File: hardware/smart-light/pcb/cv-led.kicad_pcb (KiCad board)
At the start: 2 copper layers, 95.7 x 68 mm, 46 parts, among them J1 2P 5.08mm + barrel, J2 5P 5.08mm, J3 2P 5.08mm, K1 SRD-05VDC-SL-C, Q1 AO3400 / IRLZ44N, Q2 AO3400 / IRLZ44N, Q3 AO3400 / IRLZ44N, Q4 AO3400 / IRLZ44N, Q5 S8050, SW1 Tactile 6mm, U1 ESP32-WROOM-32E (4MB), U2 AMS1117-3.3, U3 MP1584 buck

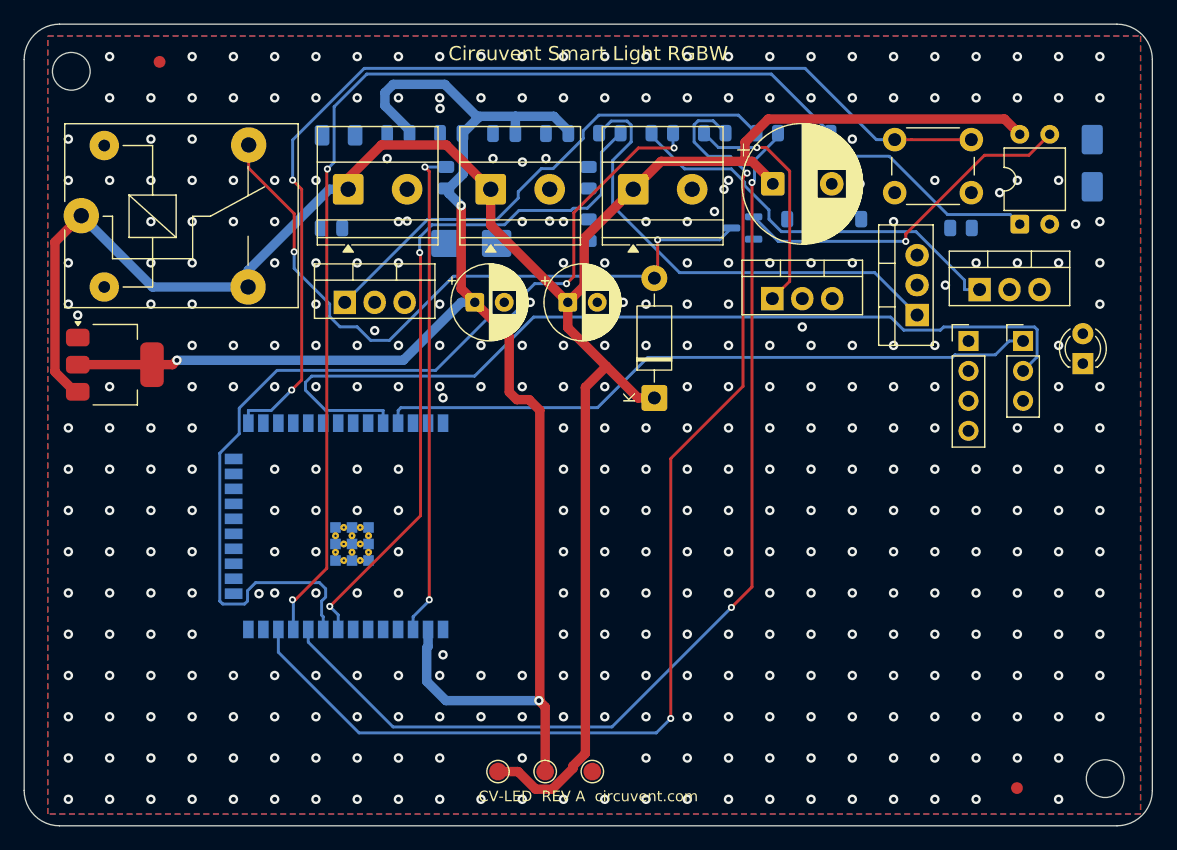
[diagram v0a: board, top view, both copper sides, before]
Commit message: hardware: fix mains isolation barrier gaps, add load-controller PCB
Adds the 13th board (ultra-compact dual-channel load controller: ESP32-C3,
opto+relay channel, MOSFET PWM channel, USB-C, AP2112K LDO, USBLC6 ESD) and
regenerates all 12 existing boards, which were stale with respect to earlier
relay-pinout and LED-polarity fixes.

The substantive change is to the mains isolation barrier. It is a keepout band
the router must not cross, deliberately cut where a component straddles it
because there the isolation is provided by the part's package. Three linked
defects made those cuts unsafe, each only visible once the previous was fixed:

1. The cut removed the barrier across the full band width for the straddling
   part's whole height, while the ISO_BRIDGE area that excuses the gap covered
   only the part itself. The router used the leftover strip beside the part to
   bring +5V within 6.99 mm of AC_N against an 8.0 mm reinforced creepage rule.
2. Straddling parts can overlap in y, so cutting per part put one part's
   keepout on another part's pads. The exempt x-ranges are now unioned per
   strip by a sweep line.
3. The rule only relaxes for items insideArea('ISO_BRIDGE'). With the hole the
   same size as the area, a track could hug the hole's edge without being
   contained in it, so the rule fired anyway and the router had no way to know.
   The hole is now the part's pad bbox + 0.3 mm, strictly inside ISO_BRIDGE at
   the footprint bbox + 0.6 mm.

The tighter hole leaves mains nets less room to reach bridge pads, so some
boards report more unconnected items. That is deliberate: those are documented
hand-routing items, whereas a creepage violation is a safety defect.

Also fixed in the generator:
- _pad_shape() derived a pad's layers from PAD::GetLayer(), which returns F.Cu
  even for pads on B.Cu. Every back-side pad became a phantom obstacle on the
  front, blocking legal paths there while hiding the real one behind. Only
  IsOnLayer() is truthful.
- Castella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
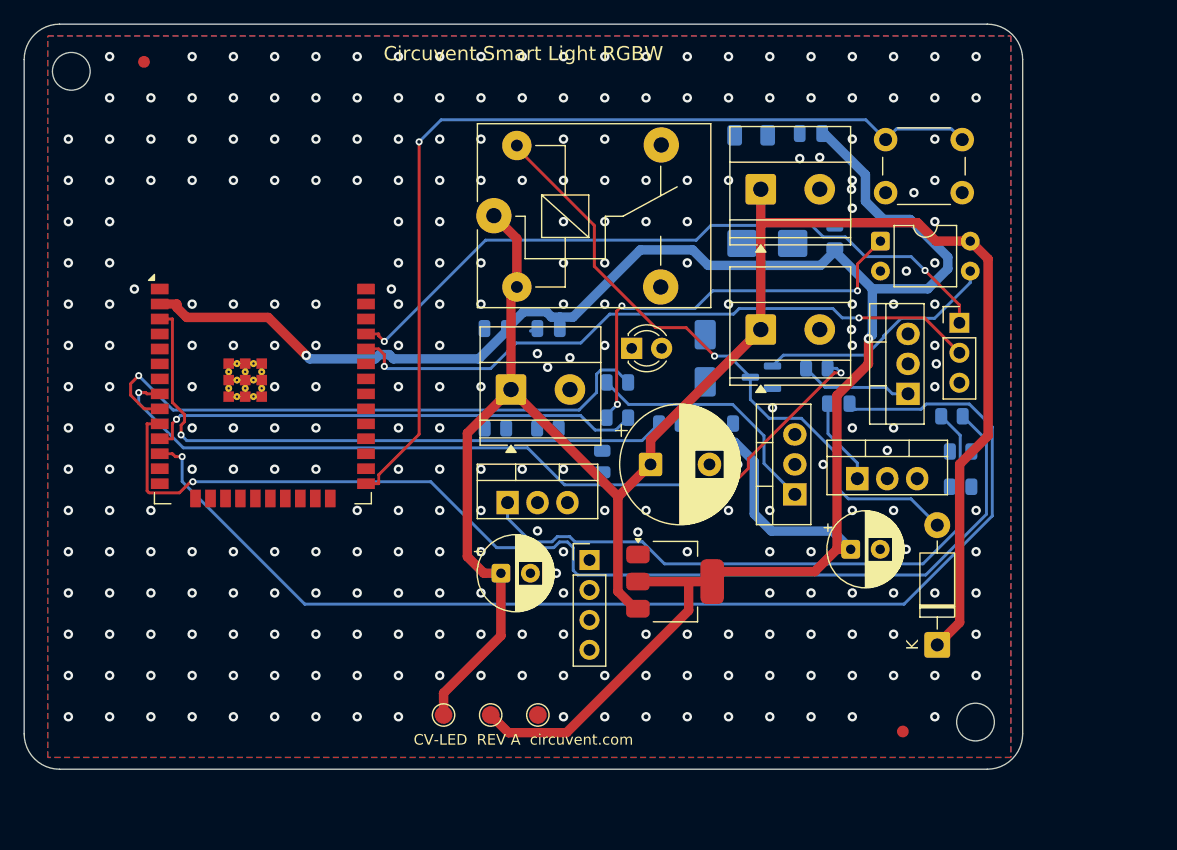
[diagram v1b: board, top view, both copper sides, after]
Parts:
- U1: moved to F.Cu
- moved R12 57.7 mm to (179.4, 119.2)
- moved U2 51.0 mm to (155.2, 127.3)
- moved LED0 38.3 mm to (151.5, 107.5), turned to 0 degrees
- moved C2 38.2 mm to (170.1, 124.5)
- moved U3 37.1 mm to (148.0, 125.5)
- moved D2 36.8 mm to (157.8, 108.3)
- moved R10 36.7 mm to (179.4, 116.2), turned to 180 degrees
- moved R11 36.3 mm to (149.0, 117.1), turned to 90 degrees
- moved J1 35.0 mm to (162.5, 94.0)
- moved C4 35.0 mm to (166.7, 89.3)
- moved K1 35.0 mm to (139.8, 96.2)
- moved F1 35.0 mm to (161.7, 89.4)
- moved C5 33.7 mm to (168.8, 98.0), turned to 90 degrees
- moved D1 31.9 mm to (177.5, 132.7)
- moved R8 31.2 mm to (140.0, 114.3)
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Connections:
- K1 pad 2: RELAY_PIN_SW -> +5V
- K1 pad 3: +5V -> RELAY_PIN_SW
- K1 pad 4: RELAY_PIN_COIL -> N$K1.4
- K1 pad 5: N$K1.5 -> RELAY_PIN_COIL
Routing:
- net RELAY_PIN: track 91.3 -> 42.3 mm, vias 2 -> 1
- net +3V3: track 135.0 -> 183.3 mm, vias 3 -> 2
- net RGB_G_PIN: track 82.2 -> 50.4 mm, vias 2 -> 1
- net RGB_R_PIN_B: track 40.4 -> 9.54 mm
- net UART_RX: track 78.1 -> 55.3 mm, vias 0 -> 2
- net +5V: track 181.1 -> 158.3 mm
- net RELAY_PIN_OPT: track 21.1 -> 35.8 mm, vias 0 -> 3
- net RGB_G_PIN_B: track 34.6 -> 21.3 mm
- net RGB_B_PIN_B: track 20.0 -> 7.40 mm, vias 1 -> 0
- net RGB_R_PIN: track 59.6 -> 70.9 mm, vias 2 -> 3
- net EN: track 41.7 -> 52.8 mm, vias 2 -> 1
- net WHITE_PWM_PIN_B: track 42.8 -> 53.0 mm
- net BTN_PIN: track 89.9 -> 79.8 mm, vias 2 -> 1
- net RELAY_PIN_DRV: track 30.1 -> 20.8 mm, vias 1 -> 0
- net WHITE_PWM_PIN: track 86.0 -> 94.5 mm, vias 2 -> 1
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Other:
- board size 95.7 x 68 mm -> 84.7 x 63.2 mm

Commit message: Release 1.10.0, and stop shipping permissions the app never uses
Cut 1.10.0 (versionCode 12) and built it: AAB 38 MB, APK 83 MB, signed with the
upload key, JS bundle embedded.

Checking the generated manifest before writing the Play listing turned up
permissions no one had asked for. Every one of them is printed on the store page
for users to read before they install:

  RECORD_AUDIO          expo-camera asks for the microphone so video can be
                        recorded with sound. This app only ever puts the camera
                        in barcode mode to read a QR label, and expo-speech is
                        output-only - it speaks, it does not listen. Left in,
                        Play lists "Microphone" against a home-control app,
                        which is alarming, unexplainable and untrue.
  SYSTEM_ALERT_WINDOW   React Native's development overlay, useless in a release
                        build and shown to users as "Display over other apps".
  READ/WRITE_EXTERNAL_STORAGE
                        Legacy storage access nothing here touches.

Stripped via android.blockedPermissions. That emits tools:node="remove", which
is a merge instruction rather than a guarantee, so it was checked against the
finished artifact with aapt2 rather than the source manifest - all four are
absent from the APK.

NEARBY_WIFI_DEVICES now carries neverForLocation. Android otherwise treats it as
location-capable, because knowing which networks are in range is enough to place
someone, and Play's data safety review treats it the same way. The app uses it
only to join a new device's setup hotspot. That flag is a promise, so the plugin
says plainly that it has to come off if scan results are ever used positionally.

What is left is defensible: location for Wi-Fi onboarding (Android requires it),
camera for the QR label, nearby-devices flagged as non-positional.

Added mobile/store/listing with the text Play asks for - title, short and full
descriptions, and what'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
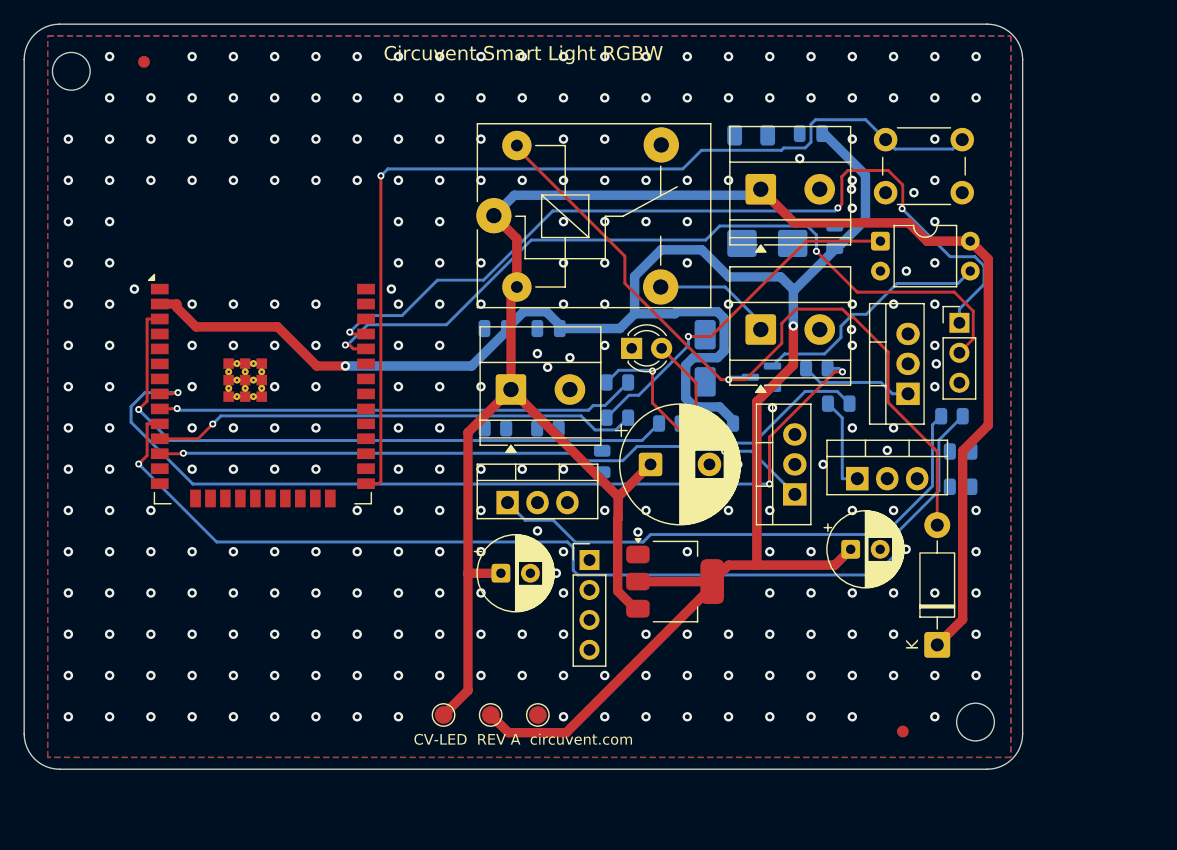
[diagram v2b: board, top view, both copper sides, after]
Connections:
- J2 pad 1: +5V -> RELAY_PIN_SW
- LED0 pad 1: N$LED0.1 -> GND
- LED0 pad 2: N$LED0.2 -> LED0_A
- R7 pad 1: N$R7.1 -> +3V3
- R7 pad 2: N$R7.2 -> LED0_A
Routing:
- net RGB_B_PIN: track 101.1 -> 61.7 mm
- net UART_TX: track 59.1 -> 72.6 mm, vias 2 -> 3
- net UART_RX: track 55.3 -> 67.2 mm
- net RELAY_PIN_COIL: track 53.9 -> 64.5 mm
- net LED0_A: track 0.00 -> 10.4 mm, vias 0 -> 1
- net RELAY_PIN_SW: track 0.00 -> 10.3 mm
- net RGB_G_PIN: track 50.4 -> 40.8 mm
- net +3V3: track 183.3 -> 175.5 mm
- net WHITE_PWM_PIN_B: track 53.0 -> 45.6 mm
- net RGB_R_PIN: track 70.9 -> 77.6 mm
- net RELAY_PIN_OPT: track 35.8 -> 29.9 mm, vias 3 -> 1
- net WHITE_PWM_PIN: track 94.5 -> 88.8 mm
- net +5V: track 158.3 -> 155.5 mm
- net EN: track 52.8 -> 54.9 mm
- net RGB_G_PIN_B: track 21.3 -> 22.3 mm, vias 0 -> 2
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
